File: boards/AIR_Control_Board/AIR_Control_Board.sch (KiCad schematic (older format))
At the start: 60 parts, among them IC1 ATMEGA16M1, J1 micromatch_female_RA_16, J2 Ultrafit_2, J3 Ultrafit_2, J4 Ultrafit_2, J5 CONN_02X03, Q1 NMOS_GSD_30V, Q2 NMOS_GSD_30V, Q3 NMOS_GSD_30V, Q4 NMOS_GSD_30V, Q5 NMOS_GSD_30V, U1 TPS561201, U2 CAN_Transceiver, Y1 Crystal_SMD

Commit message: updated air control schematic, going to work on layout soon
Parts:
- removed J1: micromatch_female_RA_16, footprints:micromatch_female_ra_16, symbol micromatch_female_RA_16
- removed J2: Ultrafit_2, footprints:Ultrafit_2, symbol Ultrafit_2-RESCUE-AIR_Control_Board
- removed Q2, Q3: NMOS_GSD_30V, TO_SOT_Packages_SMD:SOT-23, symbol NMOS_GSD_30V
- removed R1, R2: R_10k, footprints:R_0805_OEM, symbol R_10k
- removed R17, R18: R_200, footprints:R_0805_OEM, symbol R_200
- removed R5, R7: R_1k, footprints:R_0805_OEM, symbol R_1k
- removed R6, R8: R_100k, footprints:R_0805_OEM, symbol R_100k
- added D10, D11, D12, D2, D6: LED_0805, footprints:LED_0805_OEM, symbol LED_0805
- added J1: AIR-, footprints:Ultrafit_4, symbol Ultrafit_4
- added J2: Ultrafit_2, footprints:Ultrafit_2, symbol Ultrafit_2
- added J3: To Interface Board, footprints:micromatch_female_ra_18, symbol micromatch_female_RA_18
- added Q1, Q4, Q6, Q7: NMOS_GSD_30V, TO_SOT_Packages_SMD:SOT-23, symbol NMOS_GSD_30V
- added R1, R17, R18, R4, R8: R_1k, footprints:R_0805_OEM, symbol R_1k
- added R10, R19, R2, R20: R_100k, footprints:R_0805_OEM, symbol R_100k
- added R13, R21, R22, R3: R_10k, footprints:R_0805_OEM, symbol R_10k
- added R15, R28, R29, R5: R_200, footprints:R_0805_OEM, symbol R_200
- J4: renamed from J3; value Ultrafit_2 -> PrechargeRelay
- J5: renamed from J4; value Ultrafit_2 -> AIR+
- renumbered C9 to C10, C3 to C2, C10 to C3, C2 to C4, C4 to C5, C5 to C6, C6 to C7, C7 to C8, C8 to C9, D6 to D13, D11 to D14, D7 to D15, D8 to D16, D2 to D7, D9 to D8, D10 to D9, J5 to J6, Q1 to Q2, Q4 to Q3, R22 to R11, R3 to R12, R23 to R14, R11 to R16, R12 to R23, R13 to R24, R14 to R25, R15 to R26, R16 to R27, R20 to R30, R19 to R31, R21 to R32, R4 to R6, R9 to R7, R10 to R9, U2 to U1, U1 to U2
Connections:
- net labels added: AIR-_Weld_Detect, Aux_Contact+, Aux_Contact-, RXCAN, SenseConnToHVD, ShutdownSenseConnToHVD, TXCAN
- wire segments 115 -> 94
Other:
- note added: "AIR- Weld Detection"
- moved on the sheet: C1, C10, C2, C3, C4, C5, C6, C7, C8, C9, D1, D13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

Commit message: working on AIR control board, starting layout
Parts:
- Q1, Q2, Q3, Q4, Q5, Q6, Q7: footprint TO_SOT_Packages_SMD:SOT-23 -> footprints:SOT-23F
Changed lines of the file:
@@
 F 0 "Q2" H 3400 4950 50  0000 L CNN
 F 1 "NMOS_GSD_30V" V 3750 4450 50  0000 L CNN
-F 2 "TO_SOT_Packages_SMD:SOT-23" H 3700 4850 50  0001 C CNN
+F 2 "footprints:SOT-23F" H 3700 4850 50  0001 C CNN
 F 3 "https://www.digikey.com/products/en?keywords=SSM3K333RLFCT-ND" H 3700 4800 50  0001 C CNN
 F 4 "Digi-Key" H 3500 4750 60  0001 C CNN "MFN"
@@
 F 0 "Q5" H 4700 4950 50  0000 L CNN
 F 1 "NMOS_GSD_30V" V 5050 4450 50  0000 L CNN
-F 2 "TO_SOT_Packages_SMD:SOT-23" H 5000 4850 50  0001 C CNN
+F 2 "footprints:SOT-23F" H 5000 4850 50  0001 C CNN
 F 3 "https://www.digikey.com/products/en?keywords=SSM3K333RLFCT-ND" H 5000 4800 50  0001 C CNN
 F 4 "Digi-Key" H 4800 4750 60  0001 C CNN "MFN"
@@
 F 0 "Q3" V 4250 1300 50  0000 L CNN
 F 1 "NMOS_GSD_30V" V 4150 850 50  0000 L CNN
-F 2 "TO_SOT_Packages_SMD:SOT-23" H 4100 1400 50  0001 C CNN
+F 2 "footprints:SOT-23F" H 4100 1400 50  0001 C CNN
 F 3 "https://www.digikey.com/products/en?keywords=SSM3K333RLFCT-ND" H 4100 1350 50  0001 C CNN
 F 4 "Digi-Key" H 3900 1300 60  0001 C CNN "MFN"
@@
 F 0 "Q6" V 5750 1300 50  0000 L CNN
 F 1 "NMOS_GSD_30V" V 5650 850 50  0000 L CNN
-F 2 "TO_SOT_Packages_SMD:SOT-23" H 5600 1400 50  0001 C CNN
+F 2 "footprints:SOT-23F" H 5600 1400 50  0001 C CNN
 F 3 "https://www.digikey.com/products/en?keywords=SSM3K333RLFCT-ND" H 5600 1350 50  0001 C CNN
 F 4 "Digi-Key" H 5400 1300 60  0001 C CNN "MFN"
@@
 F 0 "Q4" V 4250 2800 50  0000 L CNN
 F 1 "NMOS_GSD_30V" V 4150 2350 50  0000 L CNN
-F 2 "TO_SOT_Packages_SMD:SOT-23" H 4100 2900 50  0001 C CNN
+F 2 "footprints:SOT-23F" H 4100 2900 50  0001 C CNN
 F 3 "https://www.digikey.com/products/en?keywords=SSM3K333RLFCT-ND" H 4100 2850 50  0001 C CNN
 F 4 "Digi-Key" H 3900 2800 60  0001 C CNN "MFN"
@@
 F 0 "Q7" V 5750 2800 50  0000 L CNN
 F 1 "NMOS_GSD_30V" V 5650 2350 50  0000 L CNN
-F 2 "TO_SOT_Packages_SMD:SOT-23" H 5600 2900 50  0001 C CNN
+F 2 "footprints:SOT-23F" H 5600 2900 50  0001 C CNN
 F 3 "https://www.digikey.com/products/en?keywords=SSM3K333RLFCT-ND" H 5600 2850 50  0001 C CNN
 F 4 "Digi-Key" H 5400 2800 60  0001 C CNN "MFN"
@@
 F 0 "Q1" V 2650 6750 50  0000 L CNN
 F 1 "NMOS_GSD_30V" V 2550 6300 50  0000 L CNN
-F 2 "TO_SOT_Packages_SMD:SOT-23" H 2500 6850 50  0001 C CNN
+F 2 "footprints:SOT-23F" H 2500 6850 50  0001 C CNN
 F 3 "https://www.digikey.com/products/en?keywords=SSM3K333RLFCT-ND" H 2500 6800 50  0001 C CNN
 F 4 "Digi-Key" H 2300 6750 60  0001 C CNN "MFN"

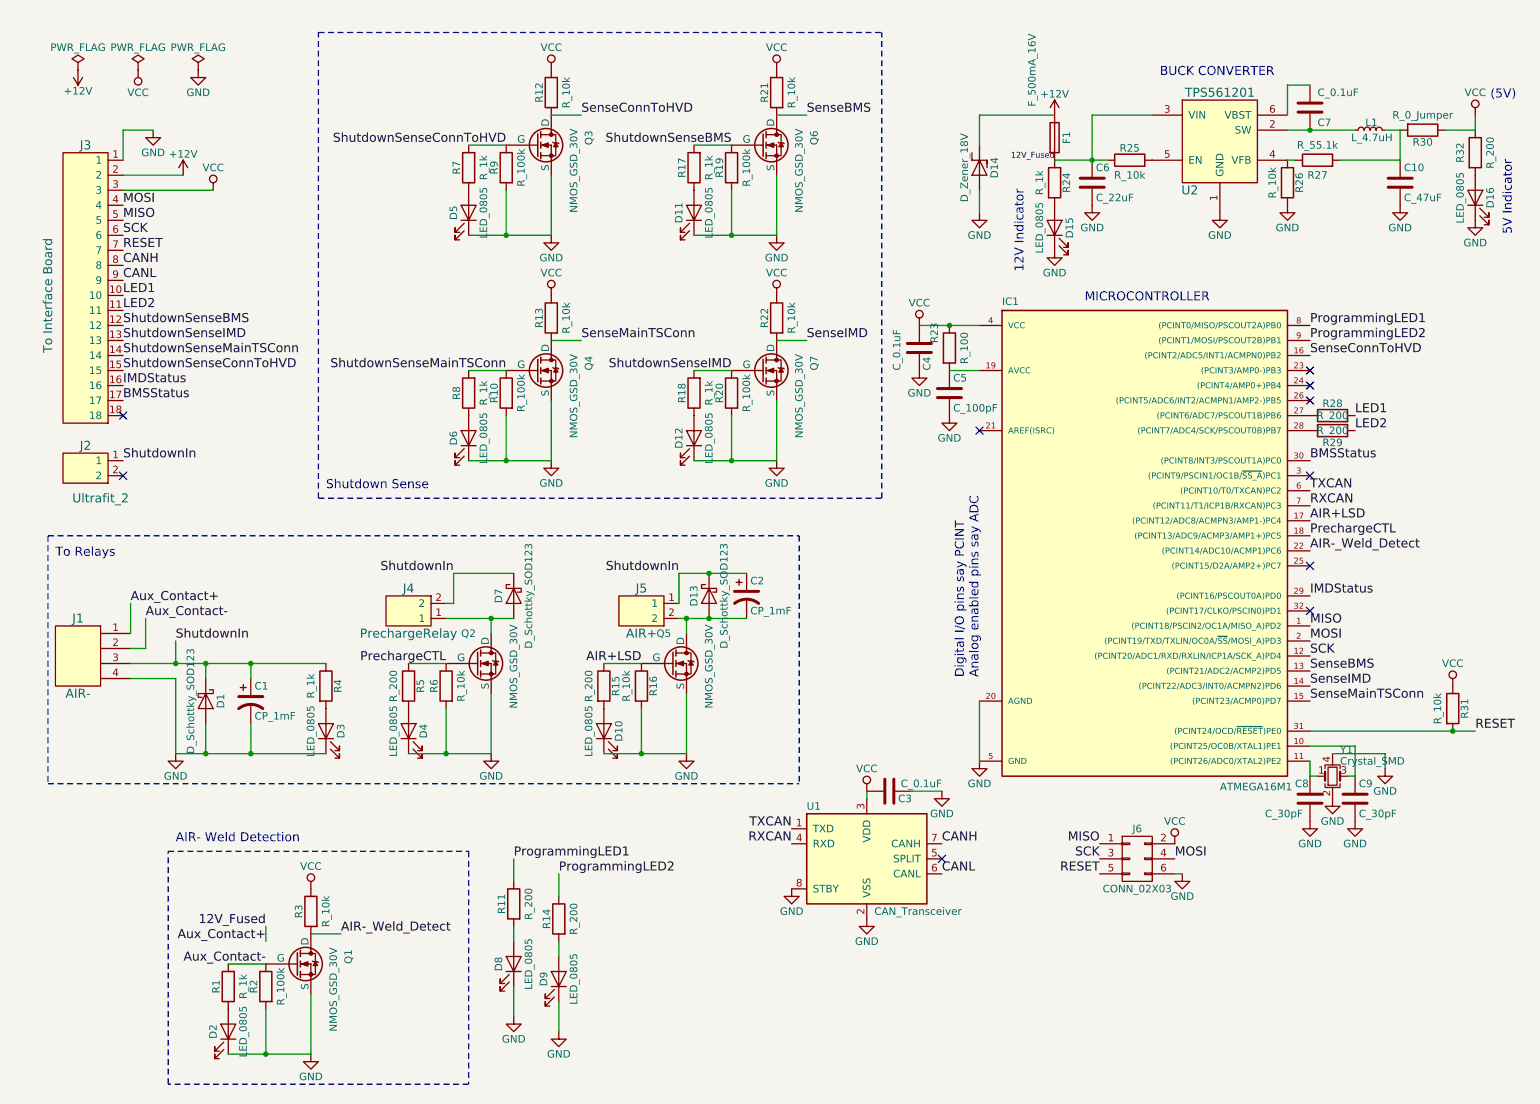
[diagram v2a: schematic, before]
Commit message: replaced all files besides BMS with most updated files from upstream
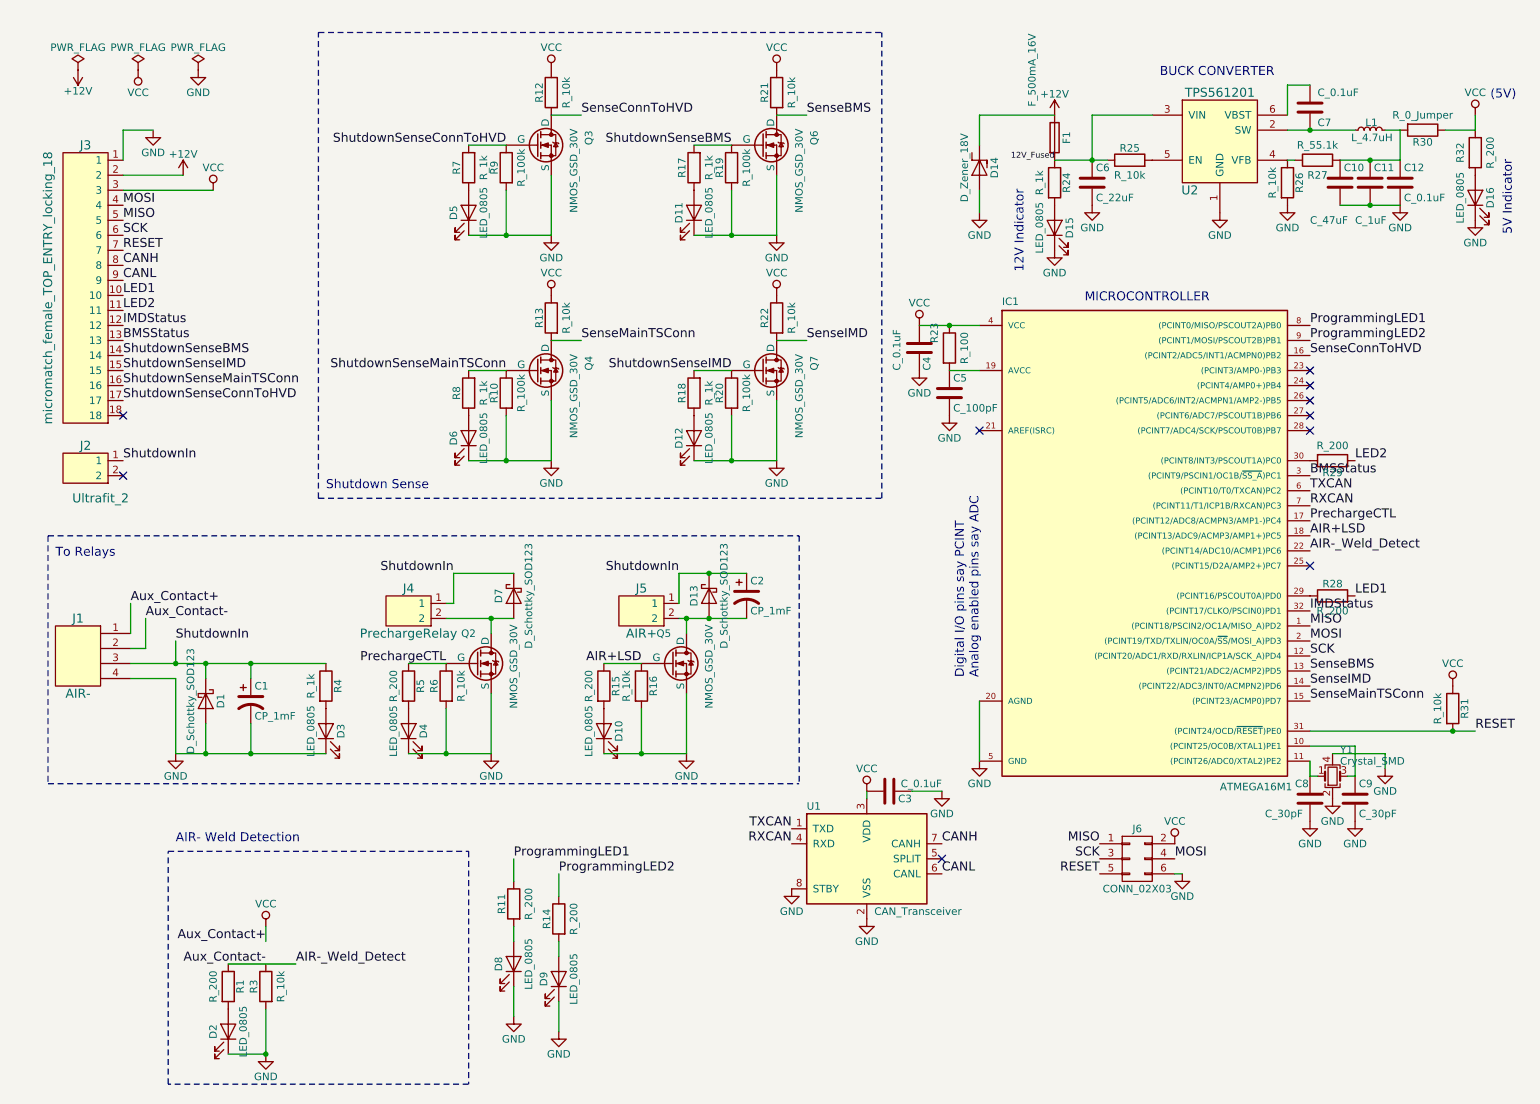
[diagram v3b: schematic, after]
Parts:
- removed J3: To Interface Board, footprints:micromatch_female_ra_18, symbol micromatch_female_RA_18
- removed Q1: NMOS_GSD_30V, footprints:SOT-23F, symbol NMOS_GSD_30V
- removed R1: R_1k, footprints:R_0805_OEM, symbol R_1k
- removed R2: R_100k, footprints:R_0805_OEM, symbol R_100k
- added C11: C_1uF, footprints:C_0805_OEM, symbol C_1uF
- added C12: C_0.1uF, footprints:C_0805_OEM, symbol C_0.1uF
- added J3: micromatch_female_TOP_ENTRY_locking_18, footprints:micromatch_female_vert_18, symbol micromatch_female_TOP_ENTRY_locking_18
- added R1: R_200, footprints:R_0805_OEM, symbol R_200
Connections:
- net Aux_Contact- is gone; now on net AIR-_Weld_Detect: J1.2
- net +12V: now also J3.2
- net 12V_Fused: no longer J1.1
- net AIR+LSD: now also IC1.18 ((PCINT13/ADC9/ACMP3/AMP1+)PC5); no longer IC1.17 ((PCINT12/ADC8/ACMPN3/AMP1-)PC4)
- net AIR-_Weld_Detect: now also R3.1, R1.1; no longer R3.2
- net BMSStatus: now also IC1.3 ((PCINT9/PSCIN1/OC1B/~SS_A~)PC1), J3.13; no longer IC1.30 ((PCINT8/INT3/PSCOUT1A)PC0)
- net CANH: now also J3.8
- net CANL: now also J3.9
- net GND: now also R3.2, C11.2, C12.2, J3.1
- net IMDStatus: now also IC1.32 ((PCINT17/CLKO/PSCIN0)PD1), J3.12; no longer IC1.29 ((PCINT16/PSCOUT0A)PD0)
- net LED1: now also J3.10
- net LED2: now also J3.11
- net MISO: now also J3.5
- net MOSI: now also J3.4
- net PrechargeCTL: now also IC1.17 ((PCINT12/ADC8/ACMPN3/AMP1-)PC4); no longer IC1.18 ((PCINT13/ADC9/ACMP3/AMP1+)PC5)
- net RESET: now also J3.7
- net SCK: now also J3.6
- net ShutdownIn: now also J4.1; no longer J4.2
- net ShutdownSenseBMS: now also J3.14
- net ShutdownSenseConnToHVD: now also J3.17
- net ShutdownSenseIMD: now also J3.15
- net ShutdownSenseMainTSConn: now also J3.16
- net VCC: now also J1.1, J3.3; no longer R3.1
- net at C10.1, L1.2, R27.2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: now also C11.1, C12.1
- net at IC1.27 ((PCINT6/ADC7/PSCOUT1B)PB6): no longer R28.1
- net at IC1.28 ((PCINT7/ADC4/SCK/PSCOUT0B)PB7): no longer R29.2
- net at D7.2 (A), Q2.3 (D): now also J4.2; no longer J4.1
- net at D2.2 (A): now also R1.2
- new net: IC1.29 ((PCINT16/PSCOUT0A)PD0), R28.1
- new net: IC1.30 ((PCINT8/INT3/PSCOUT1A)PC0), R29.2
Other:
- moved on the sheet: C10, R28, R29, R3
